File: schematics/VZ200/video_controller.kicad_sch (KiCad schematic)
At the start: 14 parts, among them U14 74LS245, U15 MC6847, U7 6116

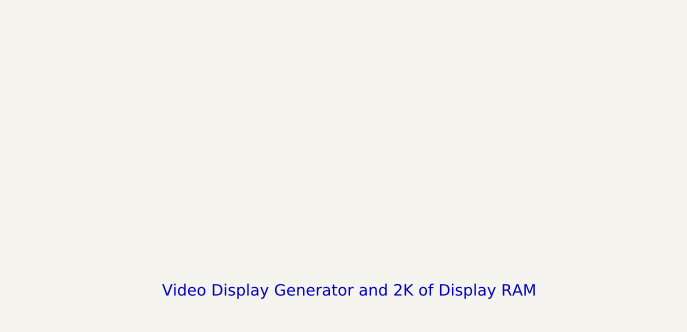
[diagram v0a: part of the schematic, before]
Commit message: Schematic for the VZ200 printer interface
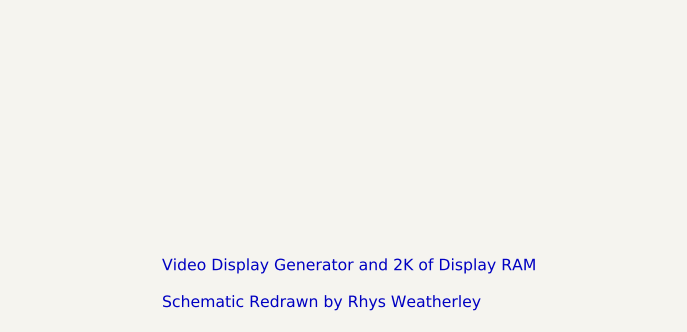
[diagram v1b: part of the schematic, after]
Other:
- note added: "Video Display Generator and 2K of Display RAM Schematic Redrawn by Rhys Weatherley"
- note removed: "Video Display Generator and 2K of Display RAM"
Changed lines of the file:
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@@
     (effects (font (size 1.27 1.27)) (justify left bottom))
   )
-  (text "Video Display Generator and 2K of Display RAM" (at 182.245 175.26 0)
+  (text "Video Display Generator and 2K of Display RAM\n\nSchematic Redrawn by Rhys Weatherley"
+    (at 182.245 176.53 0)
     (effects (font (size 1.27 1.27)) (justify left bottom))
   )

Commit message: Add title and revision details to the schematic sheets
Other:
- title: (none) -> VZ200 Computer
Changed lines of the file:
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@@
 (kicad_sch (version 20230121) (generator eeschema)
   (paper "A4")
+  (title_block
+    (title "VZ200 Computer")
+    (date "2024-01-01")
+    (rev "1")
+  )
   (junction (at 186.69 112.395) (diameter 0) (color 0 0 0 0)
   )

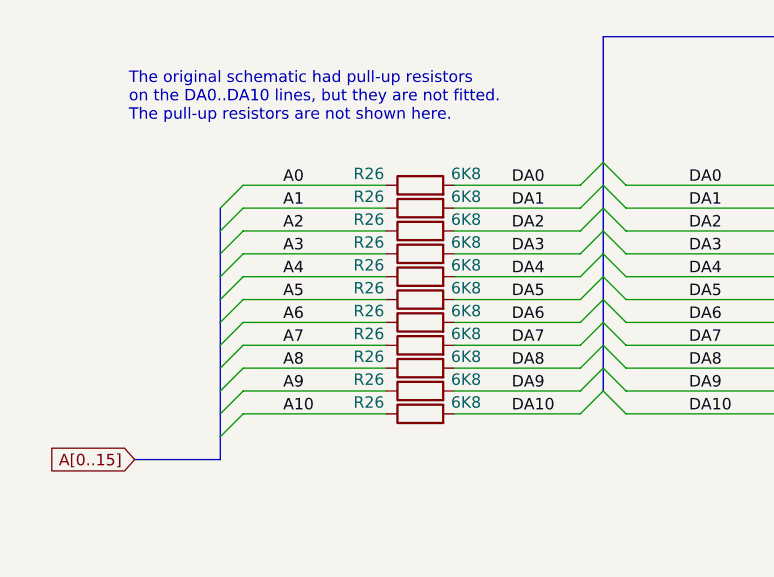
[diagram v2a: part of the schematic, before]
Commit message: Update motherboard schematic based on inspection of the actual board
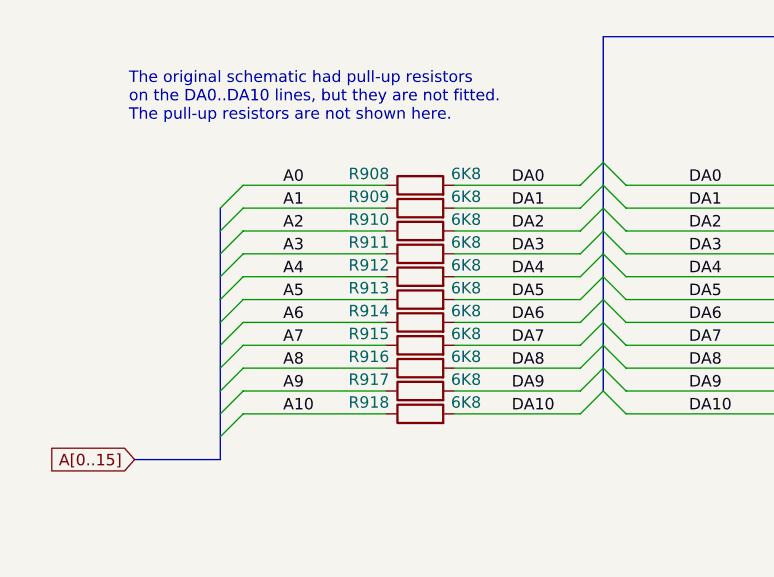
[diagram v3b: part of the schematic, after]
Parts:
- renumbered R26 to R908, R26 to R909, R26 to R910, R26 to R911, R26 to R912, R26 to R913, R26 to R914, R26 to R915, R26 to R916, R26 to R917, R26 to R918
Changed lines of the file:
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@@
   (title_block
     (title "VZ200 Computer")
-    (date "2024-01-01")
-    (rev "1")
+    (date "2024-01-05")
+    (rev "2")
   )
   (junction (at 186.69 112.395) (diameter 0) (color 0 0 0 0)
@@
   (symbol (lib_id "Device:R") (at 85.09 64.135 90) (unit 1)
     (in_bom yes) (on_board yes) (dnp no)
-    (property "Reference" "R26" (at 79.375 62.865 90)
+    (property "Reference" "R910" (at 79.375 62.865 90)
       (effects (font (size 1.27 1.27)))
     )
@@
     (instances
       (project "VZ200"
-        (path "/5e5f5998-714c-4695-b6b0-5b20d6c62fd6"
-          (reference "R26") (unit 1)
-        )
-        (path "/5e5f5998-714c-4695-b6b0-5b20d6c62fd6/6328ad0a-b5e9-48b1-85ea-8ba16c2316ca"
-          (reference "R13") (unit 1)
-        )
         (path "/5e5f5998-714c-4695-b6b0-5b20d6c62fd6/3da1966a-3153-43ad-8bb8-b6c6ea05c132"
           (reference "R910") (unit 1)
@@
   (symbol (lib_id "Device:R") (at 85.09 76.835 90) (unit 1)
     (in_bom yes) (on_board yes) (dnp no)
-    (property "Reference" "R26" (at 79.375 75.565 90)
+    (property "Reference" "R915" (at 79.375 75.565 90)
       (effects (font (size 1.27 1.27)))
     )
@@
     (instances
       (project "VZ200"
-        (path "/5e5f5998-714c-4695-b6b0-5b20d6c62fd6"
-          (reference "R26") (unit 1)
-        )
-        (path "/5e5f5998-714c-4695-b6b0-5b20d6c62fd6/6328ad0a-b5e9-48b1-85ea-8ba16c2316ca"
-          (reference "R13") (unit 1)
-        )
         (path "/5e5f5998-714c-4695-b6b0-5b20d6c62fd6/3da1966a-3153-43ad-8bb8-b6c6ea05c132"
           (reference "R915") (unit 1)
@@
   (symbol (lib_id "Device:R") (at 85.09 79.375 90) (unit 1)
     (in_bom yes) (on_board yes) (dnp no)
-    (property "Reference" "R26" (at 79.375 78.105 90)
+    (property "Reference" "R916" (at 79.375 78.105 90)
       (effects (font (size 1.27 1.27)))
     )
@@
     (instances
       (project "VZ200"
-        (path "/5e5f5998-714c-4695-b6b0-5b20d6c62fd6"
-          (reference "R26") (unit 1)
-        )
-        (path "/5e5f5998-714c-4695-b6b0-5b20d6c62fd6/6328ad0a-b5e9-48b1-85ea-8ba16c2316ca"
-          (reference "R13") (unit 1)
-        )
         (path "/5e5f5998-714c-4695-b6b0-5b20d6c62fd6/3da1966a-3153-43ad-8bb8-b6c6ea05c132"
           (reference "R916") (unit 1)
@@
   (symbol (lib_id "Device:R") (at 85.09 66.675 90) (unit 1)
     (in_bom yes) (on_board yes) (dnp no)
-    (property "Reference" "R26" (at 79.375 65.405 90)
+    (property "Reference" "R911" (at 79.375 65.405 90)
       (effects (font (size 1.27 1.27)))
     )
@@
     (instances
       (project "VZ200"
-        (path "/5e5f5998-714c-4695-b6b0-5b20d6c62fd6"
-          (reference "R26") (unit 1)
-        )
-        (path "/5e5f5998-714c-4695-b6b0-5b20d6c62fd6/6328ad0a-b5e9-48b1-85ea-8ba16c2316ca"
-          (reference "R13") (unit 1)
-        )
         (path "/5e5f5998-714c-4695-b6b0-5b20d6c62fd6/3da1966a-3153-43ad-8bb8-b6c6ea05c132"
           (reference "R911") (unit 1)
@@
   (symbol (lib_id "Device:R") (at 85.09 69.215 90) (unit 1)
     (in_bom yes) (on_board yes) (dnp no)
-    (property "Reference" "R26" (at 79.375 67.945 90)
+    (property "Reference" "R912" (at 79.375 67.945 90)
       (effects (font (size 1.27 1.27)))
     )
@@
     (instances
       (project "VZ200"
-        (path "/5e5f5998-714c-4695-b6b0-5b20d6c62fd6"
-          (reference "R26") (unit 1)
-        )
-        (path "/5e5f5998-714c-4695-b6b0-5b20d6c62fd6/6328ad0a-b5e9-48b1-85ea-8ba16c2316ca"
-          (reference "R13") (unit 1)
-        )
         (path "/5e5f5998-714c-4695-b6b0-5b20d6c62fd6/3da1966a-3153-43ad-8bb8-b6c6ea05c132"
           (reference "R912") (unit 1)
@@
   (symbol (lib_id "Device:R") (at 85.09 84.455 90) (unit 1)
     (in_bom yes) (on_board yes) (dnp no)
-    (property "Reference" "R26" (at 79.375 83.185 90)
+    (property "Reference" "R918" (at 79.375 83.185 90)
       (effects (font (size 1.27 1.27)))
     )
@@
     (instances
       (project "VZ200"
-        (path "/5e5f5998-714c-4695-b6b0-5b20d6c62fd6"
-          (reference "R26") (unit 1)
-        )
-        (path "/5e5f5998-714c-4695-b6b0-5b20d6c62fd6/6328ad0a-b5e9-48b1-85ea-8ba16c2316ca"
-          (reference "R13") (unit 1)
-        )
         (path "/5e5f5998-714c-4695-b6b0-5b20d6c62fd6/3da1966a-3153-43ad-8bb8-b6c6ea05c132"
           (reference "R918") (unit 1)
@@
   (symbol (lib_id "Device:R") (at 85.09 81.915 90) (unit 1)
     (in_bom yes) (on_board yes) (dnp no)
-    (property "Reference" "R26" (at 79.375 80.645 90)
+    (property "Reference" "R917" (at 79.375 80.645 90)
       (effects (font (size 1.27 1.27)))
     )
@@
     (instances
       (project "VZ200"
-        (path "/5e5f5998-714c-4695-b6b0-5b20d6c62fd6"
-          (reference "R26") (unit 1)
-        )
-        (path "/5e5f5998-714c-4695-b6b0-5b20d6c62fd6/6328ad0a-b5e9-48b1-85ea-8ba16c2316ca"
-          (reference "R13") (unit 1)
-        )
         (path "/5e5f5998-714c-4695-b6b0-5b20d6c62fd6/3da1966a-3153-43ad-8bb8-b6c6ea05c132"
           (reference "R917") (unit 1)
@@
   (symbol (lib_id "Device:R") (at 85.09 61.595 90) (unit 1)
     (in_bom yes) (on_board yes) (dnp no)
-    (property "Reference" "R26" (at 79.375 60.325 90)
+    (property "Reference" "R909" (at 79.375 60.325 90)
       (effects (font (size 1.27 1.27)))
     )
@@
     (instances
       (project "VZ200"
-        (path "/5e5f5998-714c-4695-b6b0-5b20d6c62fd6"
-          (reference "R26") (unit 1)
-        )
-        (path "/5e5f5998-714c-4695-b6b0-5b20d6c62fd6/6328ad0a-b5e9-48b1-85ea-8ba16c2316ca"
-          (reference "R13") (unit 1)
-        )
         (path "/5e5f5998-714c-4695-b6b0-5b20d6c62fd6/3da1966a-3153-43ad-8bb8-b6c6ea05c132"
           (reference "R909") (unit 1)
@@
   (symbol (lib_id "Device:R") (at 85.09 71.755 90) (unit 1)
     (in_bom yes) (on_board yes) (dnp no)
-    (property "Reference" "R26" (at 79.375 70.485 90)
+    (property "Reference" "R913" (at 79.375 70.485 90)
       (effects (font (size 1.27 1.27)))
     )
@@
     (instances
       (project "VZ200"
-        (path "/5e5f5998-714c-4695-b6b0-5b20d6c62fd6"
-          (reference "R26") (unit 1)
-        )
-        (path "/5e5f5998-714c-4695-b6b0-5b20d6c62fd6/6328ad0a-b5e9-48b1-85ea-8ba16c2316ca"
-          (reference "R13") (unit 1)
-        )
         (path "/5e5f5998-714c-4695-b6b0-5b20d6c62fd6/3da1966a-3153-43ad-8bb8-b6c6ea05c132"
           (reference "R913") (unit 1)
@@
   (symbol (lib_id "Device:R") (at 85.09 74.295 90) (unit 1)
     (in_bom yes) (on_board yes) (dnp no)
-    (property "Reference" "R26" (at 79.375 73.025 90)
+    (property "Reference" "R914" (at 79.375 73.025 90)
       (effects (font (size 1.27 1.27)))
     )
@@
     (instances
       (project "VZ200"
-        (path "/5e5f5998-714c-4695-b6b0-5b20d6c62fd6"
-          (reference "R26") (unit 1)
-        )
-        (path "/5e5f5998-714c-4695-b6b0-5b20d6c62fd6/6328ad0a-b5e9-48b1-85ea-8ba16c2316ca"
-          (reference "R13") (unit 1)
-        )
         (path "/5e5f5998-714c-4695-b6b0-5b20d6c62fd6/3da1966a-3153-43ad-8bb8-b6c6ea05c132"
           (reference "R914") (unit 1)
@@
   (symbol (lib_id "Device:R") (at 85.09 59.055 90) (unit 1)
     (in_bom yes) (on_board yes) (dnp no)
-    (property "Reference" "R26" (at 79.375 57.785 90)
+    (property "Reference" "R908" (at 79.375 57.785 90)
       (effects (font (size 1.27 1.27)))
     )
@@
     (instances
       (project "VZ200"
-        (path "/5e5f5998-714c-4695-b6b0-5b20d6c62fd6"
-          (reference "R26") (unit 1)
-        )
-        (path "/5e5f5998-714c-4695-b6b0-5b20d6c62fd6/6328ad0a-b5e9-48b1-85ea-8ba16c2316ca"
-          (reference "R13") (unit 1)
-        )
         (path "/5e5f5998-714c-4695-b6b0-5b20d6c62fd6/3da1966a-3153-43ad-8bb8-b6c6ea05c132"
           (reference "R908") (unit 1)
